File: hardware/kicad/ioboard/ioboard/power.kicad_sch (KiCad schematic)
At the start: 31 parts, among them J1 PWR_IN, Q5 CSD18531Q5A, U1 LM74610QDGKRQ1, U2 TVS3300DRV, U3 171013801, U4 171013801, U5 171033801, U6 R1SX-3.33.3-R, U7 RK-0515S

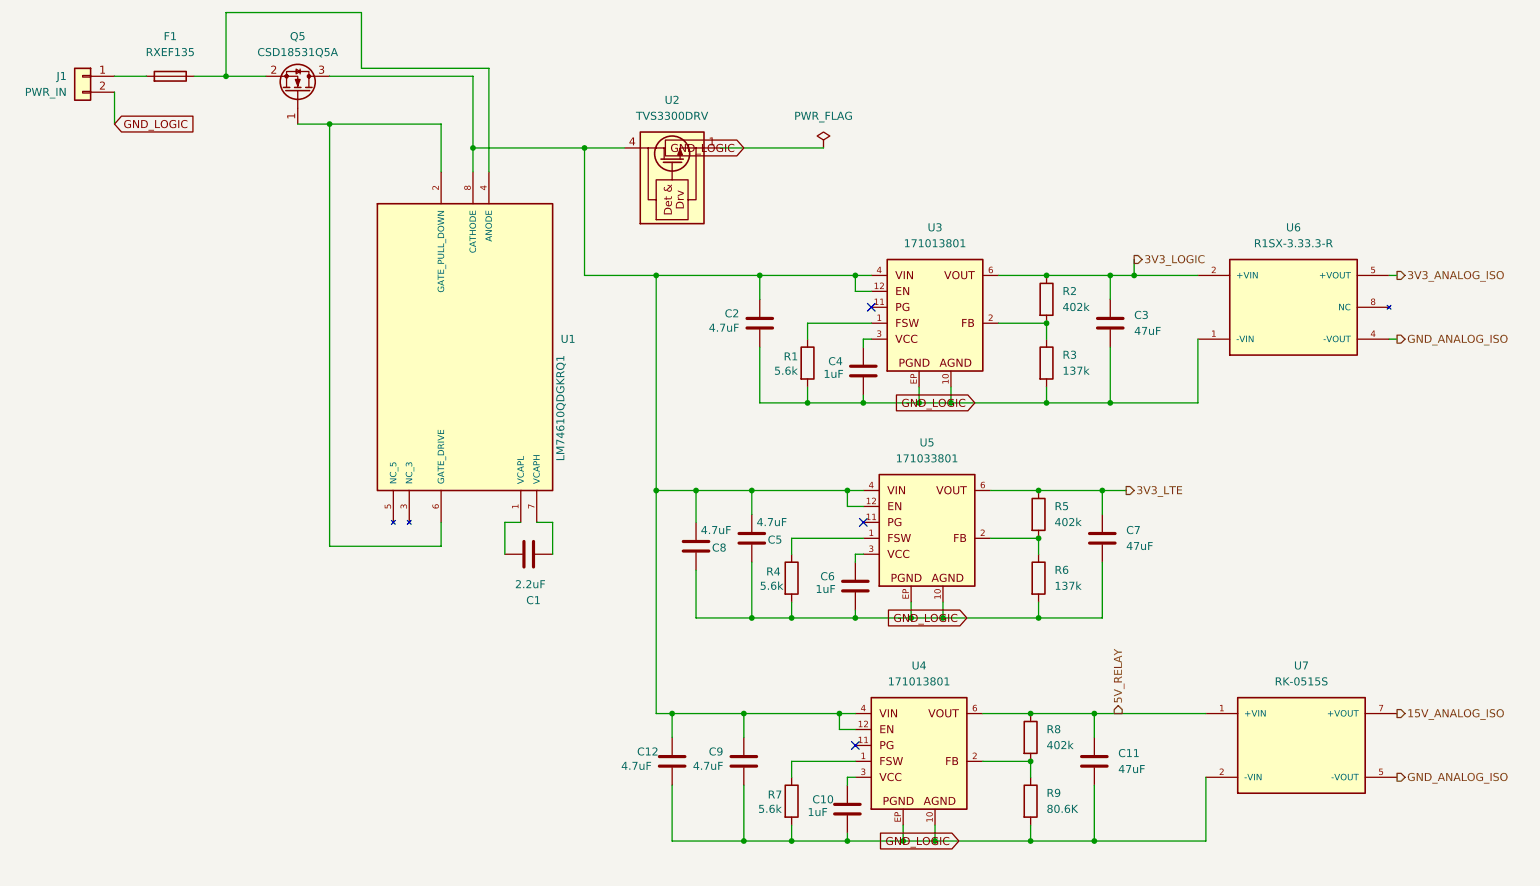
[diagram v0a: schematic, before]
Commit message: Complete LTE subsystem: schematic capture, master-sheet integration, and the VBAT_LTE rail fix
- lte.kicad_sch: modem (EG915UEUAC-N05-SNNSA), TXB0102 UART level shifter, pre-biased
  transistor PWRKEY/RESET_N drive (Q4/Q5), SIM interface + ESD protection (D1, now with
  all 4 channels wired including the SIM VDD line), antenna matching network, VBAT
  decoupling. Two schematic-level gaps found while verifying the master-sheet integration
  (D1's unwired 4th ESD channel, two missing No-Connect flags on U4) are fixed and
  re-verified against a fresh netlist reconstruction.
- lteboard.kicad_sch: LTE sheet symbol + its 6 hierarchical pins added and checked
  pin-for-pin against lte.kicad_sch's own hierarchical labels (name + direction) - exact
  match. Not yet wired into the rest of the board; that needs roadmap steps 6 (pin
  planning) and 7 (board-to-board connector), neither started.
- Carries the VBAT_LTE rail fix from 2026-09-13 that had never been committed: renamed
  from 3V3_LTE and retapped (137k -> 115k) from ~3.3V (the exact floor of Quectel's spec,
  zero margin) to ~3.82V, matching Quectel's typical - power.md, architecture.md,
  analog-io.md, and the corresponding ioboard.kicad_sch/power.kicad_sch label+value
  changes.
- Also includes an RS485_RXD/RS485_TXD pin/direction correction on ioboard.kicad_sch's
  root sheet pins, and RS232/ioboard reference-designator re-annotation (RS232's parts
  renumbered to fit the whole-board sequence), both already sitting in the working tree.
- Docs: lte.md (full build plan through Step 7), lte_bom.csv, README.md's new LTE section,
  roadmap.md's LTE line updated from "plan drafted" to done through schematic capture/BOM.
- Removed 4 stale duplicate doc files (CLAUDE-1.md, roadmap-1.md, ethernet-1.md,
  README-1.md), confirmed byte-identical to their real counterparts before deletion.

Co-Authored-By: Claude Sonnet 5 <noreply@anthropic.com>
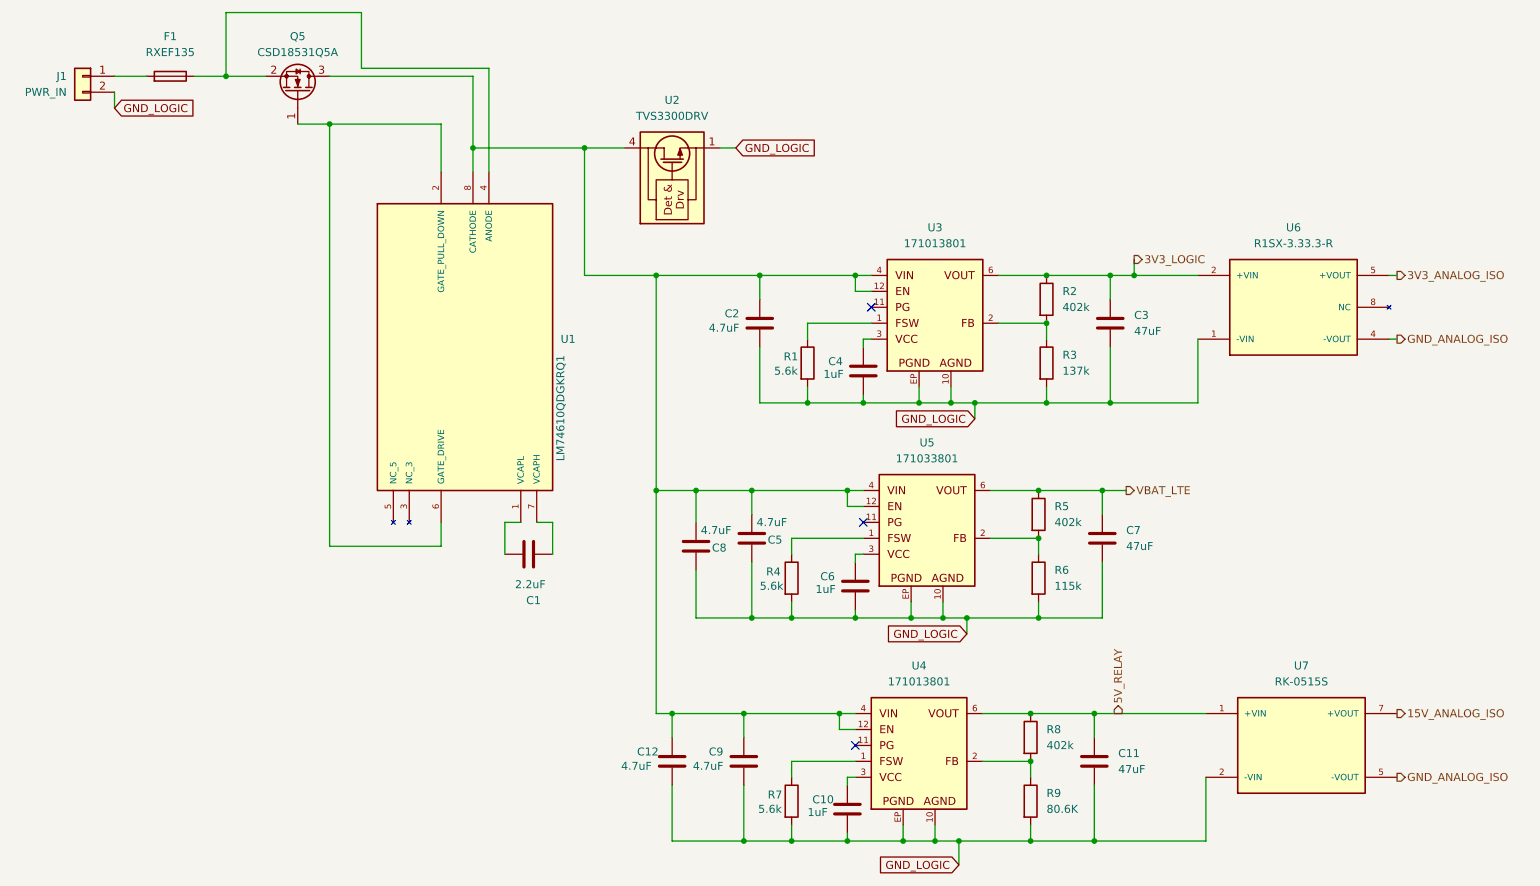
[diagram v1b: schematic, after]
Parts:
- R6: value 137k -> 115k
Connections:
- net 3V3_LTE renamed VBAT_LTE
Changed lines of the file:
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@@
+	)
+	(junction
+		(at 172.72 156.21)
+		(diameter 0)
+		(color 0 0 0 0)
 	)
 	(junction
@@
 	)
 	(junction
+		(at 173.99 120.65)
+		(diameter 0)
+		(color 0 0 0 0)
+	)
+	(junction
 		(at 139.7 100.33)
 		(diameter 0)
@@
 		(color 0 0 0 0)
 	)
+	(junction
+		(at 175.26 86.36)
+		(diameter 0)
+		(color 0 0 0 0)
+	)
 	(no_connect
 		(at 157.48 105.41)
@@
 	(wire
 		(pts
+			(xy 172.72 156.21) (xy 184.15 156.21)
+		)
+		(stroke
+			(width 0)
+			(type default)
+		)
+	)
+	(wire
+		(pts
+			(xy 172.72 160.02) (xy 172.72 156.21)
+		)
+		(stroke
+			(width 0)
+			(type default)
+		)
+	)
+	(wire
+		(pts
 			(xy 124.46 100.33) (xy 130.81 100.33)
 		)
@@
 	(wire
 		(pts
-			(xy 168.91 156.21) (xy 184.15 156.21)
+			(xy 168.91 156.21) (xy 172.72 156.21)
 		)
 		(stroke
@@
 	(wire
 		(pts
-			(xy 170.18 120.65) (xy 185.42 120.65)
+			(xy 170.18 120.65) (xy 173.99 120.65)
 		)
 		(stroke
@@
 	(wire
 		(pts
+			(xy 173.99 120.65) (xy 185.42 120.65)
+		)
+		(stroke
+			(width 0)
+			(type default)
+		)
+	)
+	(wire
+		(pts
 			(xy 158.75 73.66) (xy 148.59 73.66)
 		)
@@
 	(wire
 		(pts
-			(xy 171.45 86.36) (xy 186.69 86.36)
+			(xy 173.99 123.19) (xy 173.99 120.65)
+		)
+		(stroke
+			(width 0)
+			(type default)
+		)
+	)
+	(wire
+		(pts
+			(xy 171.45 86.36) (xy 175.26 86.36)
 		)
 		(stroke
@@
 	(wire
 		(pts
-			(xy 38.1 36.83) (xy 38.1 41.91)
+			(xy 38.1 36.83) (xy 38.1 39.37)
 		)
 		(stroke
@@
 	(wire
 		(pts
+			(xy 175.26 86.36) (xy 186.69 86.36)
+		)
+		(stroke
+			(width 0)
+			(type default)
+		)
+	)
+	(wire
+		(pts
 			(xy 62.23 34.29) (xy 55.88 34.29)
 		)
@@
 	(wire
 		(pts
+			(xy 175.26 88.9) (xy 175.26 86.36)
+		)
+		(stroke
+			(width 0)
+			(type default)
+		)
+	)
+	(wire
+		(pts
 			(xy 242.57 66.04) (xy 241.3 66.04)
 		)
@@
 	(wire
 		(pts
-			(xy 134.62 45.72) (xy 151.13 45.72)
+			(xy 134.62 45.72) (xy 137.16 45.72)
 		)
 		(stroke
@@
 	(global_label "GND_LOGIC"
 		(shape input)
-		(at 173.99 120.65 180)
+		(at 173.99 123.19 180)
 		(fields_autoplaced yes)
 		(effects
@@
 		)
 		(property "Intersheetrefs" "${INTERSHEET_REFS}"
-			(at 160.6633 120.65 0)
+			(at 160.6633 123.19 0)
 			(effects
 				(font
@@
 	(global_label "GND_LOGIC"
 		(shape input)
-		(at 38.1 41.91 0)
+		(at 38.1 39.37 0)
 		(fields_autoplaced yes)
 		(effects
@@
 		)
 		(property "Intersheetrefs" "${INTERSHEET_REFS}"
-			(at 51.4267 41.91 0)
+			(at 51.4267 39.37 0)
 			(effects
 				(font
@@
 	(global_label "GND_LOGIC"
 		(shape input)
-		(at 175.26 86.36 180)
+		(at 175.26 88.9 180)
 		(fields_autoplaced yes)
 		(effects
@@
 		)
 		(property "Intersheetrefs" "${INTERSHEET_REFS}"
-			(at 161.9333 86.36 0)
+			(at 161.9333 88.9 0)
 			(effects
 				(font
@@
 	(global_label "GND_LOGIC"
 		(shape input)
-		(at 172.72 156.21 180)
+		(at 172.72 160.02 180)
 		(fields_autoplaced yes)
 		(effects
@@
 		)
 		(property "Intersheetrefs" "${INTERSHEET_REFS}"
-			(at 159.3933 156.21 0)
+			(at 159.3933 160.02 0)
 			(effects
 				(font
@@
 	(global_label "GND_LOGIC"
 		(shape input)
-		(at 138.43 45.72 180)
+		(at 137.16 45.72 0)
 		(fields_autoplaced yes)
 		(effects
@@
 				(size 1.27 1.27)
 			)
-			(justify right)
+			(justify left)
 		)
 		(property "Intersheetrefs" "${INTERSHEET_REFS}"
-			(at 125.1033 45.72 0)
-			(effects
-				(font
-					(size 1.27 1.27)
-				)
-				(justify right)
+			(at 150.4867 45.72 0)
+			(effects
+				(font
+					(size 1.27 1.27)
+				)
+				(justify left)
 				(hide yes)
 			)
@@
 		)
 	)
-	(hierarchical_label "3V3_LTE"
+	(hierarchical_label "VBAT_LTE"
 		(shape output)
 		(at 199.39 100.33 0)
@@
 			)
 		)
-		(property "Value" "137k"
+		(property "Value" "115k"
 			(at 187.96 115.5699 0)
 			(effects
@@
 					(unit 1)
 				)
-			)
-		)
-	)
-	(symbol
-		(lib_id "power:PWR_FLAG")
-		(at 151.13 45.72 0)
-		(unit 1)
-		(exclude_from_sim no)
-		(in_bom yes)
-		(on_board yes)
-		(dnp no)
-		(fields_autoplaced yes)
-		(property "Reference" "#FLG01"
-			(at 151.13 43.815 0)
-			(effects
-				(font
-					(size 1.27 1.27)
-				)
-				(hide yes)
-			)
-		)
-		(property "Value" "PWR_FLAG"
-			(at 151.13 40.64 0)
-			(effects
-				(font
-					(size 1.27 1.27)
-				)
-			)
-		)
-		(property "Footprint" ""
-			(at 151.13 45.72 0)
-			(effects
-				(font
-					(size 1.27 1.27)
-				)
-				(hide yes)
-			)
-		)
-		(property "Datasheet" "~"
-			(at 151.13 45.72 0)
-			(effects
-				(font
-					(size 1.27 1.27)
-				)
-				(hide yes)
-			)
-		)
-		(property "Description" "Special symbol for telling ERC where power comes from"
-			(at 151.13 45.72 0)
-			(effects
-				(font
-					(size 1.27 1.27)
-				)
-				(hide yes)
-			)
-		)
-		(pin "1"
-		)
-		(instances
-			(project ""
-				(path "/a0fa9f92-ef51-408b-9617-1545f9e9dad8/9bc843cc-645c-4034-a877-ed0cc8bfa13d"
-					(reference "#FLG01")
-					(unit 1)
-				)
-			)
-			(project "power"
-				(path "/f922969b-7ad0-4b87-b465-c564dde21786"
-					(reference "#FLG01")
-					(unit 1)
-				)
